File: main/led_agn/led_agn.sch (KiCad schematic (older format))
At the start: 164 parts, among them J1 Barrel_Jack_Switch, J2 Power_Terminal, Q1 BS250, Q2 2N7000, Q3 2N7000, Q4 2N7000, Q5 2N7000, Q6 2N7000, Q7 2N7000, Q8 2N7000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

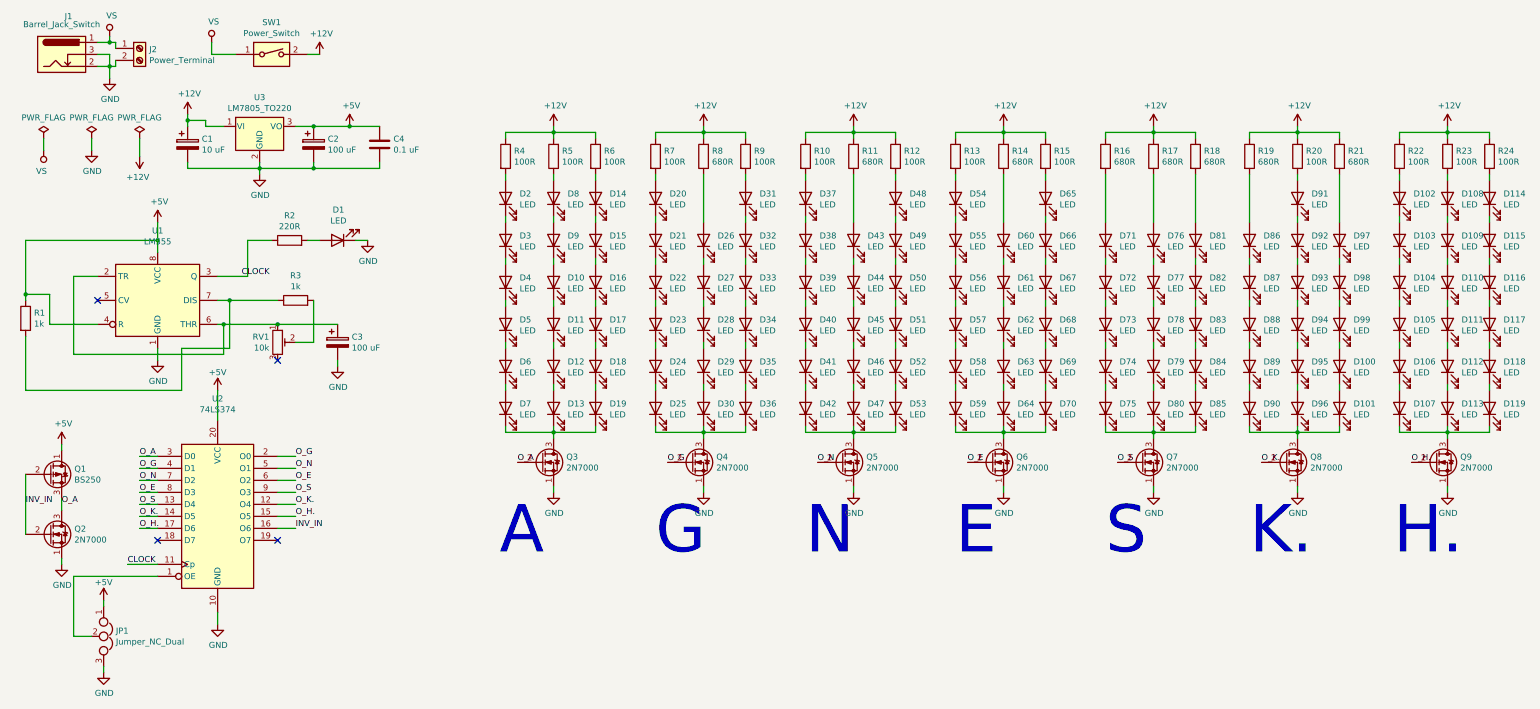
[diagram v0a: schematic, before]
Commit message: add already-placed design (before routing)
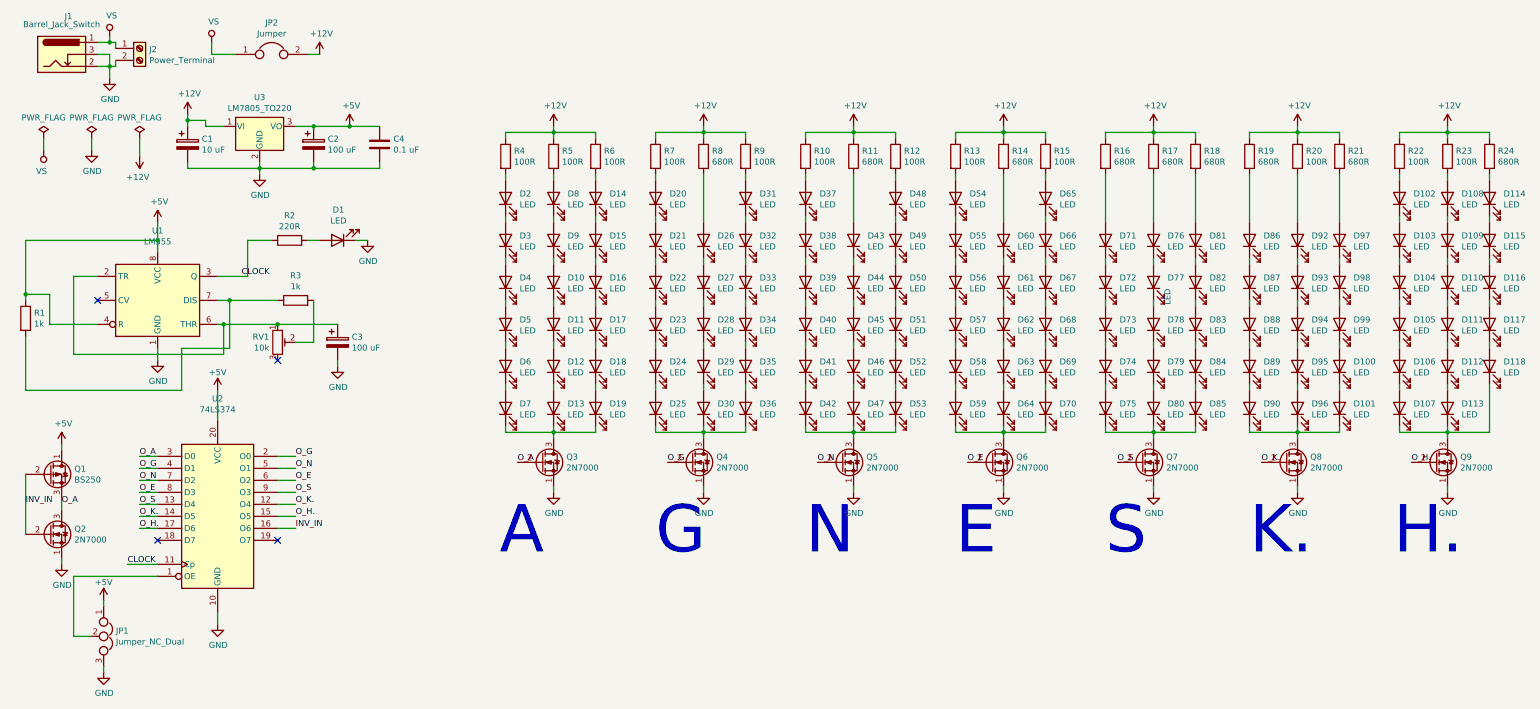
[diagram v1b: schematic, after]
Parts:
- removed D119, D91: LED, LED_THT:LED_D3.0mm, symbol Device:LED
- removed SW1: Power_Switch, symbol Switch:SW_DIP_x01
- added JP2: Jumper, Connector_PinHeader_2.54mm:PinHeader_1x02_P2.54mm_Vertical, symbol Device:Jumper
- R24: value 100R -> 680R
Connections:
- net +12V: now also JP2.2
- net VS: now also JP2.1
- net at D92.2 (A): now also R20.1
- net at D107.1 (K), D113.1 (K), Q9.3 (D): now also D118.1 (K)
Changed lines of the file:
@@
-$EndComp
-$Comp
-L Device:LED D70
-U 1 1 5D8671BC
-P 9050 3800
-F 0 "D70" V 9089 3683 50  0000 R CNN
-F 1 "LED" V 8998 3683 50  0000 R CNN
-F 2 "LED_THT:LED_D3.0mm" H 9050 3800 50  0001 C CNN
-F 3 "~" H 9050 3800 50  0001 C CNN
-	1    9050 3800
-	0    -1   -1   0
 $EndComp
 $Comp
@@
 P 9950 2750
 F 0 "D77" V 9989 2633 50  0000 R CNN
-F 1 "LED" V 9898 2633 50  0000 R CNN
+F 1 "LED" H 9898 2633 50  0000 R CNN
 F 2 "LED_THT:LED_D3.0mm" H 9950 2750 50  0001 C CNN
 F 3 "~" H 9950 2750 50  0001 C CNN
@@
 S\n
 $Comp
-L Device:LED D91
-U 1 1 5D8EE926
-P 11150 2050
-F 0 "D91" V 11189 1933 50  0000 R CNN
-F 1 "LED" V 11098 1933 50  0000 R CNN
-F 2 "LED_THT:LED_D3.0mm" H 11150 2050 50  0001 C CNN
-F 3 "~" H 11150 2050 50  0001 C CNN
-	1    11150 2050
-	0    -1   -1   0
-$EndComp
-$Comp
 L Device:LED D87
 U 1 1 5D8EE92C
@@
 $EndComp
 $Comp
-L Device:LED D109
-U 1 1 5D915967
-P 12400 2400
-F 0 "D109" V 12439 2283 50  0000 R CNN
-F 1 "LED" V 12348 2283 50  0000 R CNN
-F 2 "LED_THT:LED_D3.0mm" H 12400 2400 50  0001 C CNN
-F 3 "~" H 12400 2400 50  0001 C CNN
-	1    12400 2400
-	0    -1   -1   0
-$EndComp
-$Comp
 L Device:LED D110
 U 1 1 5D91596D
@@
 F 3 "~" H 12400 3800 50  0001 C CNN
 	1    12400 3800
-	0    -1   -1   0
-$EndComp
-$Comp
-L Device:LED D119
-U 1 1 5D915985
-P 12750 3800
-F 0 "D119" V 12789 3683 50  0000 R CNN
-F 1 "LED" V 12698 3683 50  0000 R CNN
-F 2 "LED_THT:LED_D3.0mm" H 12750 3800 50  0001 C CNN
-F 3 "~" H 12750 3800 50  0001 C CNN
-	1    12750 3800
 	0    -1   -1   0
 $EndComp
@@
 $EndComp
 $Comp
-L Device:R R24
-U 1 1 5D9159B5
-P 12750 1700
-F 0 "R24" H 12820 1746 50  0000 L CNN
-F 1 "100R" H 12820 1655 50  0000 L CNN
-F 2 "Resistor_THT:R_Axial_DIN0207_L6.3mm_D2.5mm_P10.16mm_Horizontal" V 12680 1700 50  0001 C CNN
-F 3 "~" H 12750 1700 50  0001 C CNN
-	1    12750 1700
-	1    0    0    -1
-$EndComp
-$Comp
 L Device:Q_NMOS_SGD Q9
 U 1 1 5D9159BC
@@
 	12400 3600 12400 3650
 Wire Wire Line
-	12750 3600 12750 3650
-Wire Wire Line
-	12750 3950 12750 4000
-Wire Wire Line
 	12750 4000 12400 4000
 Wire Wire Line
@@
 	10750 2550 10750 2600
 Wire Wire Line
-	11150 2200 11150 2250
-Wire Wire Line
 	10750 2250 10750 1850
-Wire Wire Line
-	11150 1850 11150 1900
 Wire Wire Line
 	11500 1850 11500 2250
@@
 NoConn ~ 2650 3400
 $Comp
-L Switch:SW_DIP_x01 SW1
-U 1 1 5D7DFE3E
-P 2600 850
-F 0 "SW1" H 2600 1117 50  0000 C CNN
-F 1 "Power_Switch" H 2600 1026 50  0000 C CNN
-F 2 "" H 2600 850 50  0001 C CNN
-F 3 "~" H 2600 850 50  0001 C CNN
-	1    2600 850
-	1    0    0    -1
-$EndComp
-$Comp
 L Device:LED D55
 U 1 1 5D867186
@@
 	0    -1   -1   0
 $EndComp
+$Comp
+L Device:LED D70
+U 1 1 5D8671BC
+P 9050 3800
+F 0 "D70" V 9089 3683 50  0000 R CNN
+F 1 "LED" V 8998 3683 50  0000 R CNN
+F 2 "LED_THT:LED_D3.0mm" H 9050 3800 50  0001 C CNN
+F 3 "~" H 9050 3800 50  0001 C CNN
+	1    9050 3800
+	0    -1   -1   0
+$EndComp
+$Comp
+L Device:LED D109
+U 1 1 5D915967
+P 12400 2400
+F 0 "D109" V 12439 2283 50  0000 R CNN
+F 1 "LED" V 12348 2283 50  0000 R CNN
+F 2 "LED_THT:LED_D3.0mm" H 12400 2400 50  0001 C CNN
+F 3 "~" H 12400 2400 50  0001 C CNN
+	1    12400 2400
+	0    -1   -1   0
+$EndComp
+Wire Wire Line
+	12750 3600 12750 4000
+$Comp
+L Device:R R24
+U 1 1 5D9159B5
+P 12750 1700
+F 0 "R24" H 12820 1746 50  0000 L CNN
+F 1 "680R" H 12820 1655 50  0000 L CNN
+F 2 "Resistor_THT:R_Axial_DIN0207_L6.3mm_D2.5mm_P10.16mm_Horizontal" V 12680 1700 50  0001 C CNN
+F 3 "~" H 12750 1700 50  0001 C CNN
+	1    12750 1700
+	1    0    0    -1
+$EndComp
+$Comp
+L Device:Jumper JP2
+U 1 1 5D918CE7
+P 2600 850
+F 0 "JP2" H 2600 1114 50  0000 C CNN
+F 1 "Jumper" H 2600 1023 50  0000 C CNN
+F 2 "Connector_PinHeader_2.54mm:PinHeader_1x02_P2.54mm_Vertical" H 2600 850 50  0001 C CNN
+F 3 "~" H 2600 850 50  0001 C CNN
+	1    2600 850
+	1    0    0    -1
+$EndComp
+Wire Wire Line
+	11150 1850 11150 2250
 $EndSCHEMATC
